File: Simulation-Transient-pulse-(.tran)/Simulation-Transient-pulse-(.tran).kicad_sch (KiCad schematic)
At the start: 3 parts

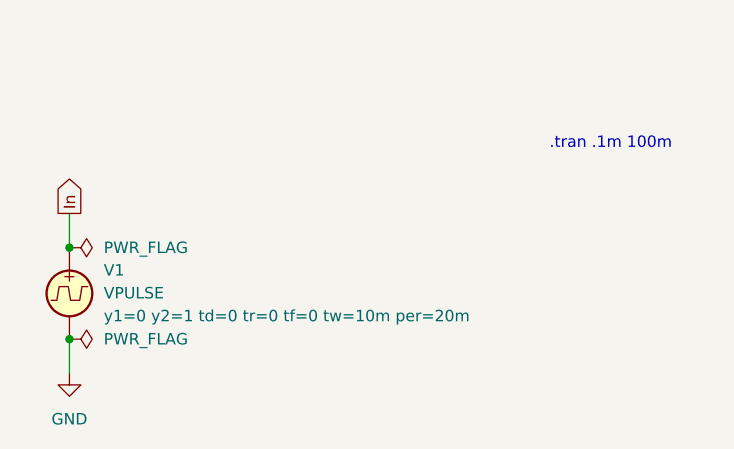
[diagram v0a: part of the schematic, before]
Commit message: Updated all schematics and prepared for KiCad 8.0
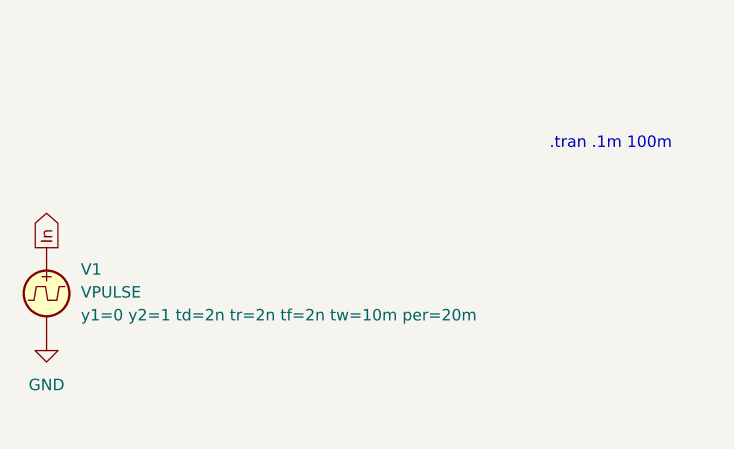
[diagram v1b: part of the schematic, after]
